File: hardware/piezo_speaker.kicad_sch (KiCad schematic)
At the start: 4 parts, among them Q2 2N3904

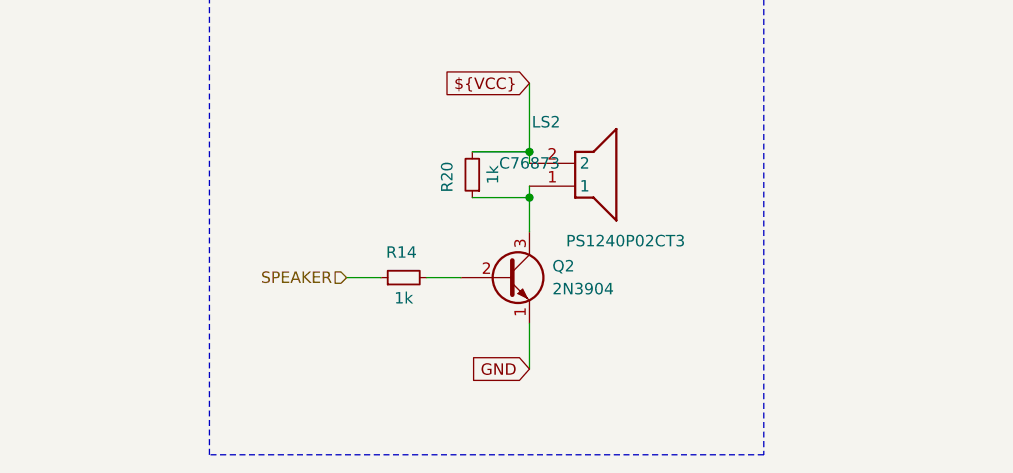
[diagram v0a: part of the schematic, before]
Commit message: Completed the property teble except for the cyristal oscilator
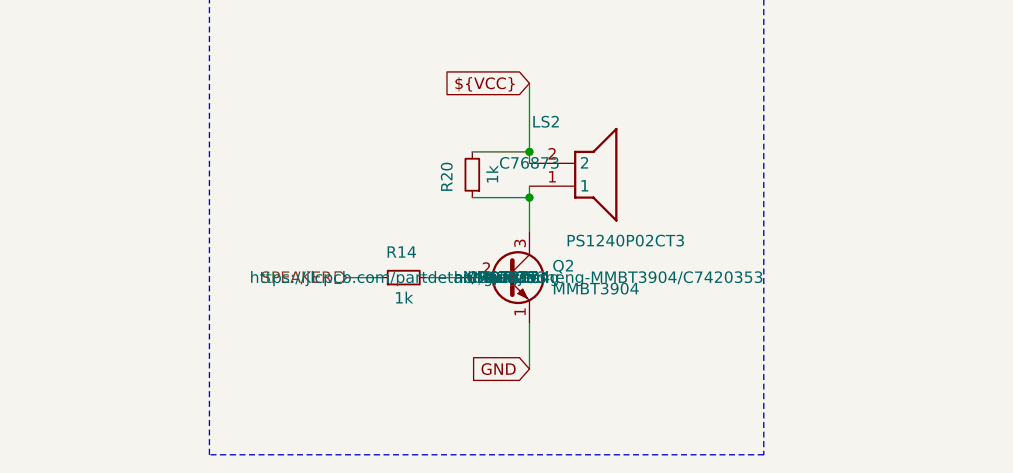
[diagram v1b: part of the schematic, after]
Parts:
- Q2: value 2N3904 -> MMBT3904; footprint Package_TO_SOT_THT:TO-92_Inline -> Package_TO_SOT_SMD:SOT-23; Manuf. Name (none) -> hongjiacheng; Manuf. Part # (none) -> MMBT3904; Package (none) -> SOT-23; Supplier Link (none) -> https://jlcpcb.com/partdetail/Hongjiacheng-MMBT3904/C7420353; Supplier Name (none) -> JLCPCB; Supplier Part # (none) -> C7420353; Supplier Unit Price (none) -> $0.0077
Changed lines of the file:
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@@
 			)
 		)
-		(property "Value" "2N3904"
+		(property "Value" "MMBT3904"
 			(at 152.4 104.1399 0)
 			(effects
@@
 			)
 		)
-		(property "Footprint" "Package_TO_SOT_THT:TO-92_Inline"
+		(property "Footprint" "Package_TO_SOT_SMD:SOT-23"
 			(at 152.4 104.775 0)
 			(effects
@@
 			)
 		)
-		(property "Datasheet" "https://www.onsemi.com/pub/Collateral/2N3903-D.PDF"
+		(property "Datasheet" "https://jlcpcb.com/api/file/downloadByFileSystemAccessId/8564879385946705920"
 			(at 147.32 102.87 0)
 			(effects
@@
 			)
 		)
-		(property "Description" "0.2A Ic, 40V Vce, Small Signal NPN Transistor, TO-92"
+		(property "Description" "40V 200mW 100@10mA,1.0V 200mA NPN SOT-23 Bipolar (BJT) ROHS"
 			(at 147.32 102.87 0)
 			(effects
@@
 			)
 		)
-		(property "Supplier Name" ""
+		(property "Supplier Name" "JLCPCB"
 			(at 147.32 102.87 0)
 			(effects
@@
 			)
 		)
+		(property "Manuf. Name" "hongjiacheng"
+			(at 147.32 102.87 0)
+			(effects
+				(font
+					(size 1.27 1.27)
+				)
+			)
+		)
+		(property "Manuf. Part #" "MMBT3904"
+			(at 147.32 102.87 0)
+			(effects
+				(font
+					(size 1.27 1.27)
+				)
+			)
+		)
+		(property "Package" "SOT-23"
+			(at 147.32 102.87 0)
+			(effects
+				(font
+					(size 1.27 1.27)
+				)
+			)
+		)
+		(property "Supplier Link" "https://jlcpcb.com/partdetail/Hongjiacheng-MMBT3904/C7420353"
+			(at 147.32 102.87 0)
+			(effects
+				(font
+					(size 1.27 1.27)
+				)
+			)
+		)
+		(property "Supplier Part #" " C7420353"
+			(at 147.32 102.87 0)
+			(effects
+				(font
+					(size 1.27 1.27)
+				)
+			)
+		)
+		(property "Supplier Unit Price" "$0.0077"
+			(at 147.32 102.87 0)
+			(effects
+				(font
+					(size 1.27 1.27)
+				)
+			)
+		)

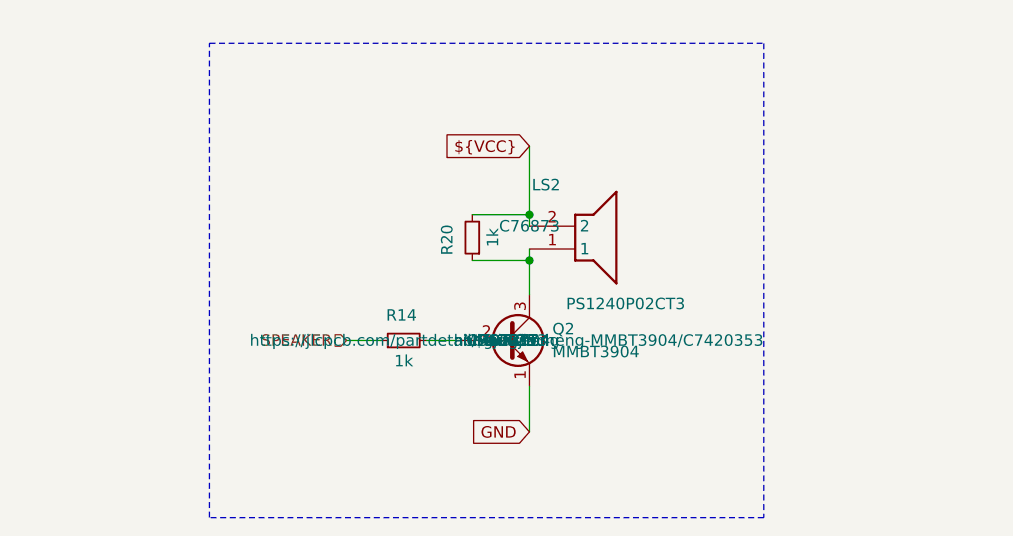
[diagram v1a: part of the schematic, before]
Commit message: Made some small changes on the properties of some components while having last weeks meeting and added the fp-info-cache to the gitignore file
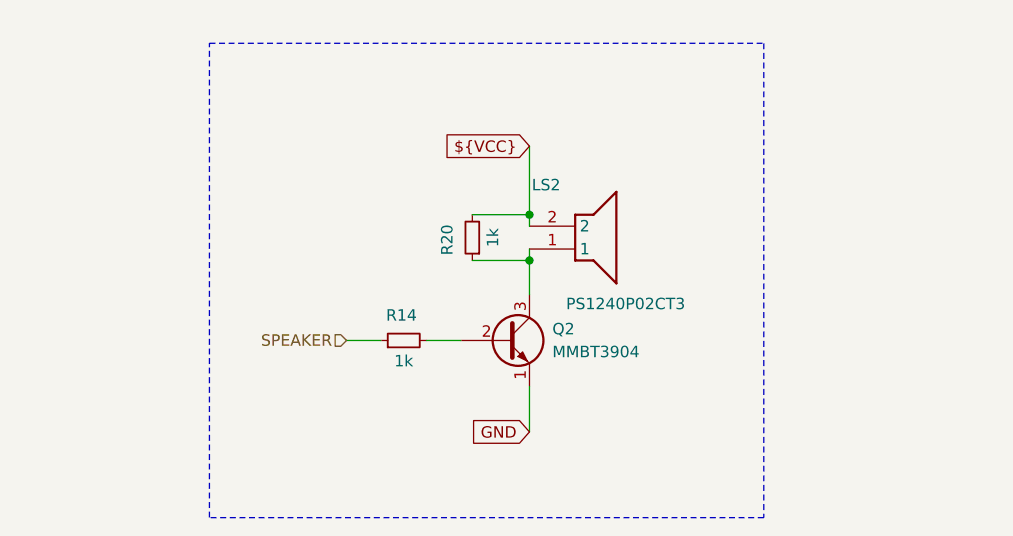
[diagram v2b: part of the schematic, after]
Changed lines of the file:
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@@
 					(size 1.27 1.27)
 				)
+				(hide yes)
 			)
 		)
@@
 					(size 1.27 1.27)
 				)
+				(hide yes)
 			)
 		)
@@
 					(size 1.27 1.27)
 				)
+				(hide yes)
 			)
 		)
@@
 					(size 1.27 1.27)
 				)
+				(hide yes)
 			)
 		)
@@
 					(size 1.27 1.27)
 				)
+				(hide yes)
 			)
 		)
@@
 					(size 1.27 1.27)
 				)
+				(hide yes)
 			)
 		)
@@
 					(size 1.27 1.27)
 				)
-			)
-		)
+				(hide yes)
+			)
+		)

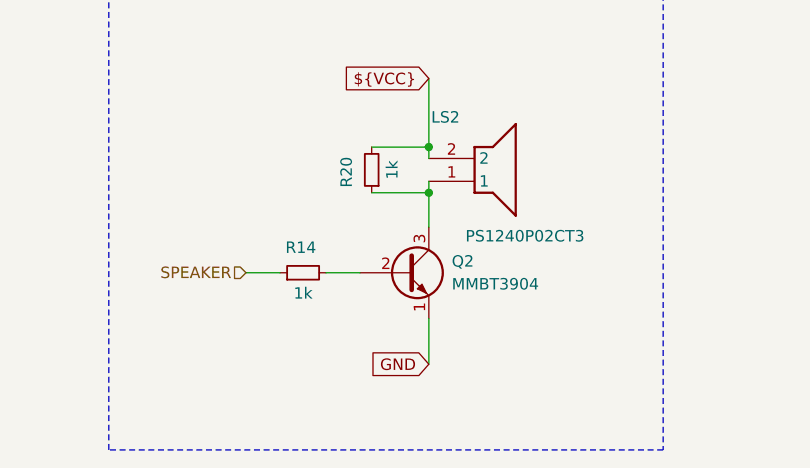
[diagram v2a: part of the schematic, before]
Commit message: Symbols pins vs footprint pins checked
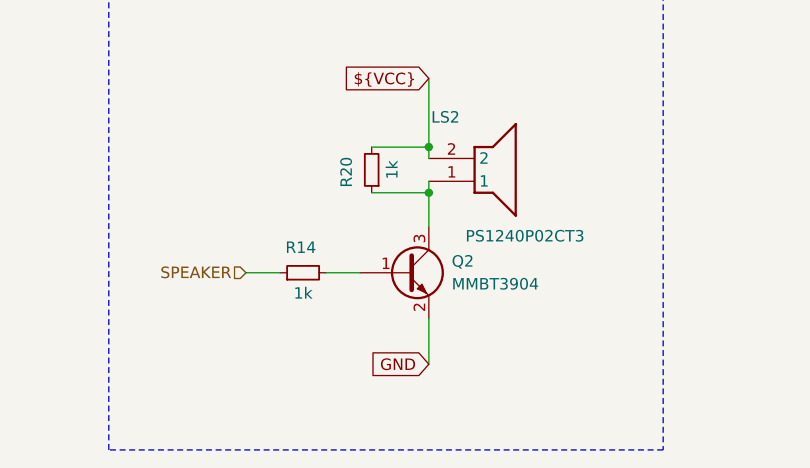
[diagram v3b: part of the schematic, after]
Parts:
- Q2: footprint Package_TO_SOT_SMD:SOT-23 -> kitchen_timer:MMBT3904 (SOT-23)
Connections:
- net GND: now also Q2.2 (E); no longer Q2.1 (E)
- net at R14.2: now also Q2.1 (B); no longer Q2.2 (B)
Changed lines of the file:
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@@
 			)
 		)
-		(property "Description" "1k, 0805"
+		(property "Description" "Resistor, small symbol"
 			(at 143.51 91.44 0)
 			(effects
@@
 			)
 		)
-		(property "Description" "1k, 0805"
+		(property "Description" "Resistor, small symbol"
 			(at 135.89 102.87 0)
 			(effects
@@
 			)
 		)
-		(property "Footprint" "Package_TO_SOT_SMD:SOT-23"
+		(property "Footprint" "kitchen_timer:MMBT3904 (SOT-23)"
 			(at 152.4 104.775 0)
 			(effects
@@
 			(at 147.32 102.87 0)
 			(effects
+				(font
+					(size 1.27 1.27)
+				)
+				(hide yes)
+			)
+		)
+		(property "Part Num" ""
+			(at 147.32 102.87 0)
+			(effects

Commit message: Electric Rules Check completed.
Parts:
- LS2: symbol kitchen_timer-symbols_lib:HNB09A05 -> kitchen_timer-symbols_lib:PS1240P02CT3; now in the parts list
- Q2: symbol Transistor_BJT:2N3904 -> kitchen_timer-symbols_lib:2N3904
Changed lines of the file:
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@@
 	)
 	(symbol
-		(lib_id "kitchen_timer-symbols_lib:HNB09A05")
+		(lib_id "kitchen_timer-symbols_lib:PS1240P02CT3")
 		(at 149.86 90.17 0)
 		(unit 1)
 		(exclude_from_sim no)
-		(in_bom no)
+		(in_bom yes)
 		(on_board yes)
 		(dnp no)
@@
 	)
 	(symbol
-		(lib_id "Transistor_BJT:2N3904")
+		(lib_id "kitchen_timer-symbols_lib:2N3904")
 		(at 147.32 102.87 0)
 		(unit 1)

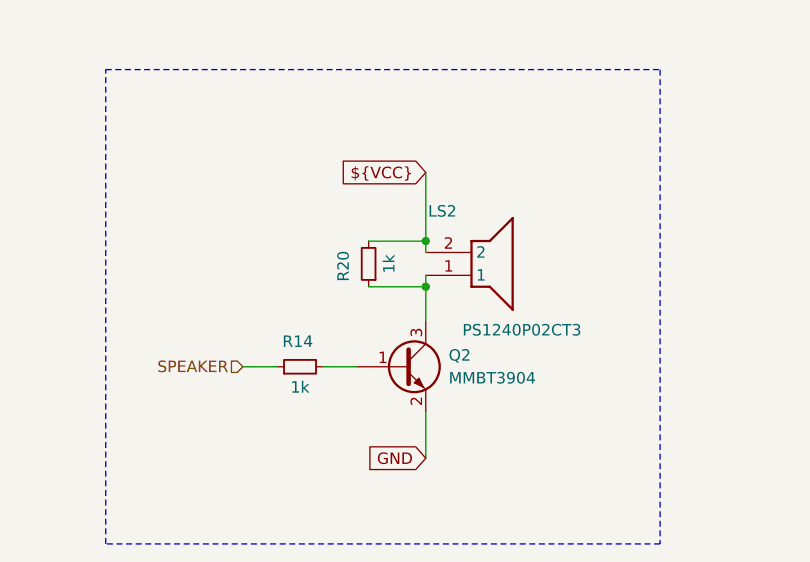
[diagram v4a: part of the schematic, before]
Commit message: Added footprints to mounting holes and selected a part for the test LED.
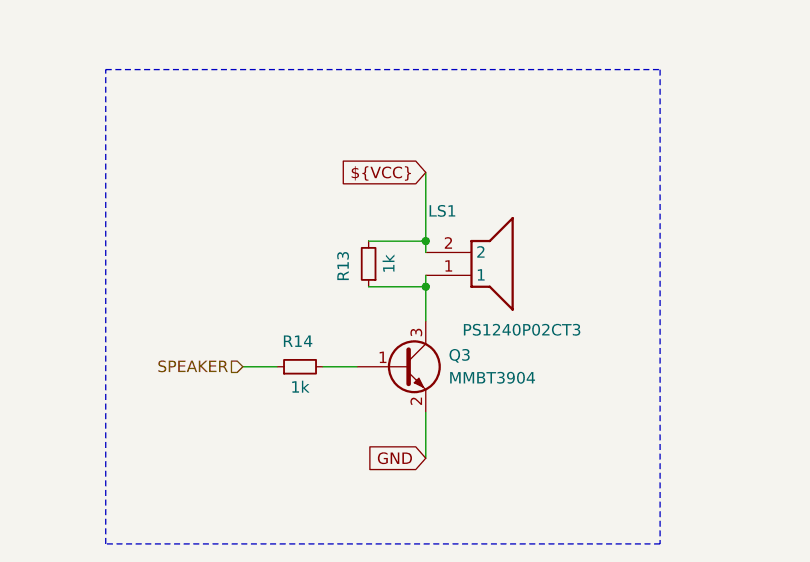
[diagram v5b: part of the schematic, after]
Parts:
- renumbered LS2 to LS1, Q2 to Q3, R20 to R13
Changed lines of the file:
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@@
 		(on_board yes)
 		(dnp no)
-		(property "Reference" "LS2"
+		(property "Reference" "LS1"
 			(at 150.114 85.598 0)
 			(effects
@@
 				)
 				(hide yes)
+			)
+		)
+		(property "Manufacturer_Name" ""
+			(at 149.86 90.17 0)
+			(effects
+				(font
+					(size 1.27 1.27)
+				)
+			)
+		)
+		(property "Manufacturer_Part_Number" ""
+			(at 149.86 90.17 0)
+			(effects
+				(font
+					(size 1.27 1.27)
+				)
+			)
+		)
+		(property "Mouser Part Number" ""
+			(at 149.86 90.17 0)
+			(effects
+				(font
+					(size 1.27 1.27)
+				)
+			)
+		)
+		(property "Mouser Price/Stock" ""
+			(at 149.86 90.17 0)
+			(effects
+				(font
+					(size 1.27 1.27)
+				)
 			)
 		)
@@
 			(project ""
 				(path "/8963deea-96bc-4401-b671-98fbe9ed9c6a/cc0cdeb4-aa65-40c1-8591-40f3174b886f"
-					(reference "LS2")
+					(reference "LS1")
 					(unit 1)
 				)
@@
 		(on_board yes)
 		(dnp no)
-		(property "Reference" "R20"
+		(property "Reference" "R13"
 			(at 140.716 91.694 90)
 			(effects
@@
 				)
 				(hide yes)
+			)
+		)
+		(property "Manufacturer_Name" ""
+			(at 143.51 91.44 0)
+			(effects
+				(font
+					(size 1.27 1.27)
+				)
+			)
+		)
+		(property "Manufacturer_Part_Number" ""
+			(at 143.51 91.44 0)
+			(effects
+				(font
+					(size 1.27 1.27)
+				)
+			)
+		)
+		(property "Mouser Part Number" ""
+			(at 143.51 91.44 0)
+			(effects
+				(font
+					(size 1.27 1.27)
+				)
+			)
+		)
+		(property "Mouser Price/Stock" ""
+			(at 143.51 91.44 0)
+			(effects
+				(font
+					(size 1.27 1.27)
+				)
 			)
 		)
@@
 			(project "kitchen_timer-hardware"
 				(path "/8963deea-96bc-4401-b671-98fbe9ed9c6a/cc0cdeb4-aa65-40c1-8591-40f3174b886f"
-					(reference "R20")
+					(reference "R13")
 					(unit 1)
 				)
@@
 			)
 		)
+		(property "Manufacturer_Name" ""
+			(at 135.89 102.87 0)
+			(effects
+				(font
+					(size 1.27 1.27)
+				)
+			)
+		)
+		(property "Manufacturer_Part_Number" ""
+			(at 135.89 102.87 0)
+			(effects
+				(font
+					(size 1.27 1.27)
+				)
+			)
+		)
+		(property "Mouser Part Number" ""
+			(at 135.89 102.87 0)
+			(effects
+				(font
+					(size 1.27 1.27)
+				)
+			)
+		)
+		(property "Mouser Price/Stock" ""
+			(at 135.89 102.87 0)
+			(effects
+				(font
+					(size 1.27 1.27)
+				)
+			)
+		)
 		(pin "1"
 		)
@@
 		(dnp no)
 		(fields_autoplaced yes)
-		(property "Reference" "Q2"
+		(property "Reference" "Q3"
 			(at 152.4 101.5999 0)
 			(effects
@@
 				)
 				(hide yes)
+			)
+		)
+		(property "Manufacturer_Name" ""
+			(at 147.32 102.87 0)
+			(effects
+				(font
+					(size 1.27 1.27)
+				)
+			)
+		)
+		(property "Manufacturer_Part_Number" ""
+			(at 147.32 102.87 0)
+			(effects
+				(font
+					(size 1.27 1.27)
+				)
+			)
+		)
+		(property "Mouser Part Number" ""
+			(at 147.32 102.87 0)
+			(effects
+				(font
+					(size 1.27 1.27)
+				)
+			)
+		)
+		(property "Mouser Price/Stock" ""
+			(at 147.32 102.87 0)
+			(effects
+				(font
+					(size 1.27 1.27)
+				)
 			)
 		)
@@
 			(project ""
 				(path "/8963deea-96bc-4401-b671-98fbe9ed9c6a/cc0cdeb4-aa65-40c1-8591-40f3174b886f"
-					(reference "Q2")
+					(reference "Q3")
 					(unit 1)
 				)

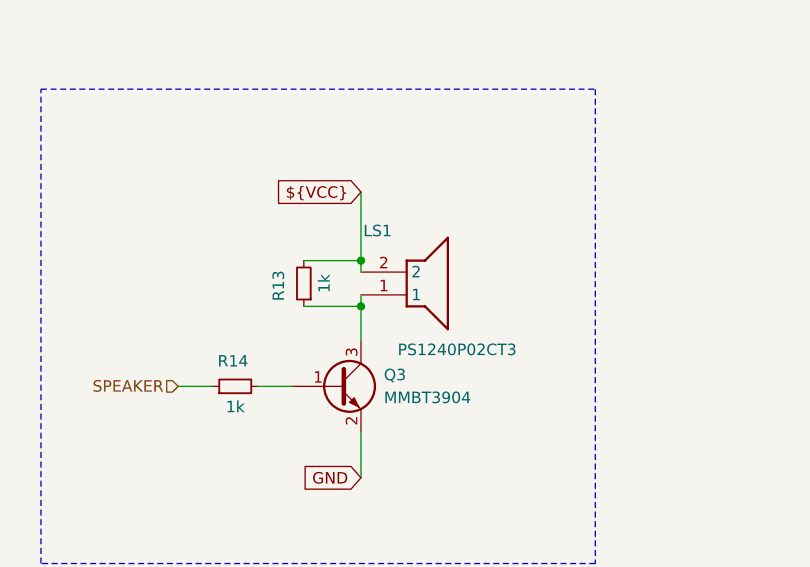
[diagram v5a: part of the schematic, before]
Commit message: Made some items DNP and/or Exclude form Board
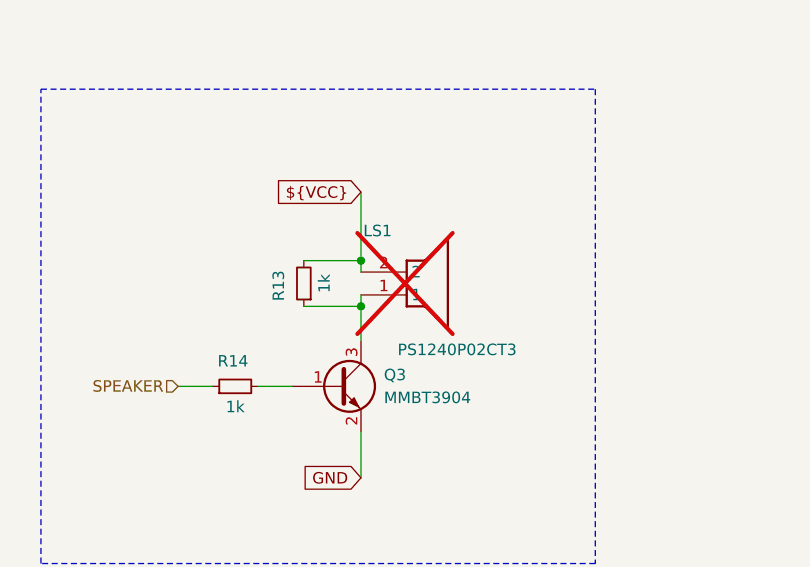
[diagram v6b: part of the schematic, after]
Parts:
- LS1: now not fitted
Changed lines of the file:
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@@
 		(in_bom yes)
 		(on_board yes)
-		(dnp no)
+		(dnp yes)
 		(property "Reference" "LS1"
 			(at 150.114 85.598 0)

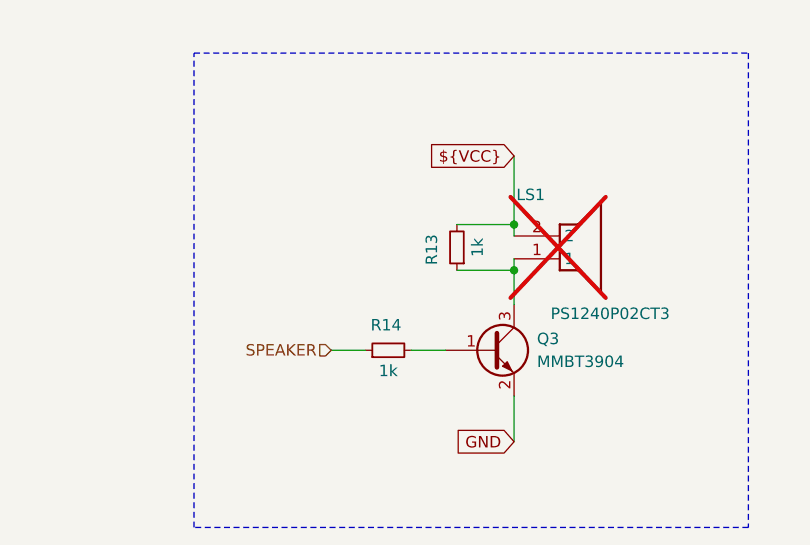
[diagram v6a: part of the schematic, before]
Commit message: Added a pull up resistor to the CS line on the SPI and added two more test LEDs
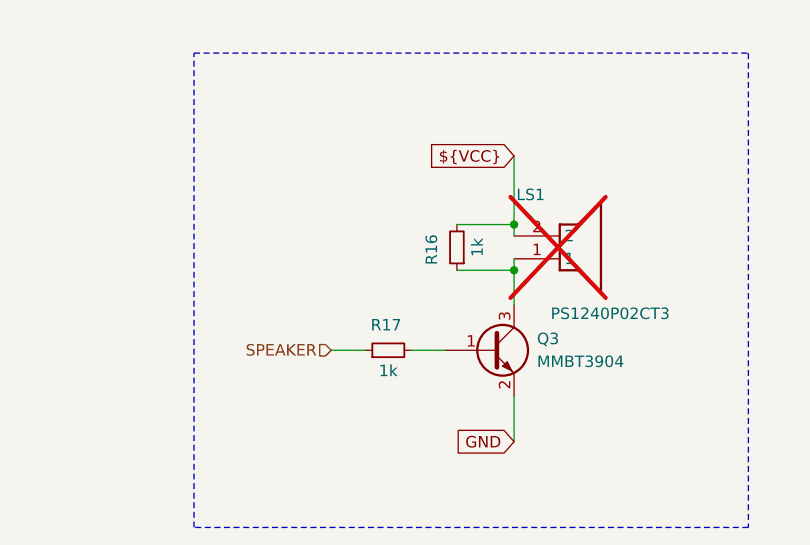
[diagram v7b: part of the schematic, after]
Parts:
- renumbered R13 to R16, R14 to R17
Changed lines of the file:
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@@
 					(size 1.27 1.27)
 				)
+				(hide yes)
 			)
 		)
@@
 					(size 1.27 1.27)
 				)
+				(hide yes)
 			)
 		)
@@
 					(size 1.27 1.27)
 				)
+				(hide yes)
 			)
 		)
@@
 					(size 1.27 1.27)
 				)
+				(hide yes)
 			)
 		)
@@
 		(on_board yes)
 		(dnp no)
-		(property "Reference" "R13"
+		(property "Reference" "R16"
 			(at 140.716 91.694 90)
 			(effects
@@
 					(size 1.27 1.27)
 				)
+				(hide yes)
 			)
 		)
@@
 					(size 1.27 1.27)
 				)
+				(hide yes)
 			)
 		)
@@
 					(size 1.27 1.27)
 				)
+				(hide yes)
 			)
 		)
@@
 					(size 1.27 1.27)
 				)
+				(hide yes)
 			)
 		)
@@
 			(project "kitchen_timer-hardware"
 				(path "/8963deea-96bc-4401-b671-98fbe9ed9c6a/cc0cdeb4-aa65-40c1-8591-40f3174b886f"
-					(reference "R13")
+					(reference "R16")
 					(unit 1)
 				)
@@
 		(on_board yes)
 		(dnp no)
-		(property "Reference" "R14"
+		(property "Reference" "R17"
 			(at 135.636 100.076 90)
 			(effects
@@
 					(size 1.27 1.27)
 				)
+				(hide yes)
 			)
 		)
@@
 					(size 1.27 1.27)
 				)
+				(hide yes)
 			)
 		)
@@
 					(size 1.27 1.27)
 				)
+				(hide yes)
 			)
 		)
@@
 					(size 1.27 1.27)
 				)
+				(hide yes)
 			)
 		)
@@
 			(project "kitchen_timer-hardware"
 				(path "/8963deea-96bc-4401-b671-98fbe9ed9c6a/cc0cdeb4-aa65-40c1-8591-40f3174b886f"
-					(reference "R14")
+					(reference "R17")
 					(unit 1)
 				)
@@
 					(size 1.27 1.27)
 				)
+				(hide yes)
 			)
 		)
@@
 					(size 1.27 1.27)
 				)
+				(hide yes)
 			)
 		)
@@
 					(size 1.27 1.27)
 				)
+				(hide yes)
 			)
 		)
@@
 					(size 1.27 1.27)
 				)
-			)
-		)
+				(hide yes)
+			)
+		)
